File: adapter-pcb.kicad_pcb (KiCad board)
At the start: 2 copper layers, 90.2 x 95.9 mm, 27 parts, among them J1 SS5-80-3.50-L-D-K-TR, J2 DM3BT-DSF-PEJS, J3 Conn_02x05_Odd_Even, U1 TXS0102QDCURQ1, U2 LTC4300A-1IMS8_PBF

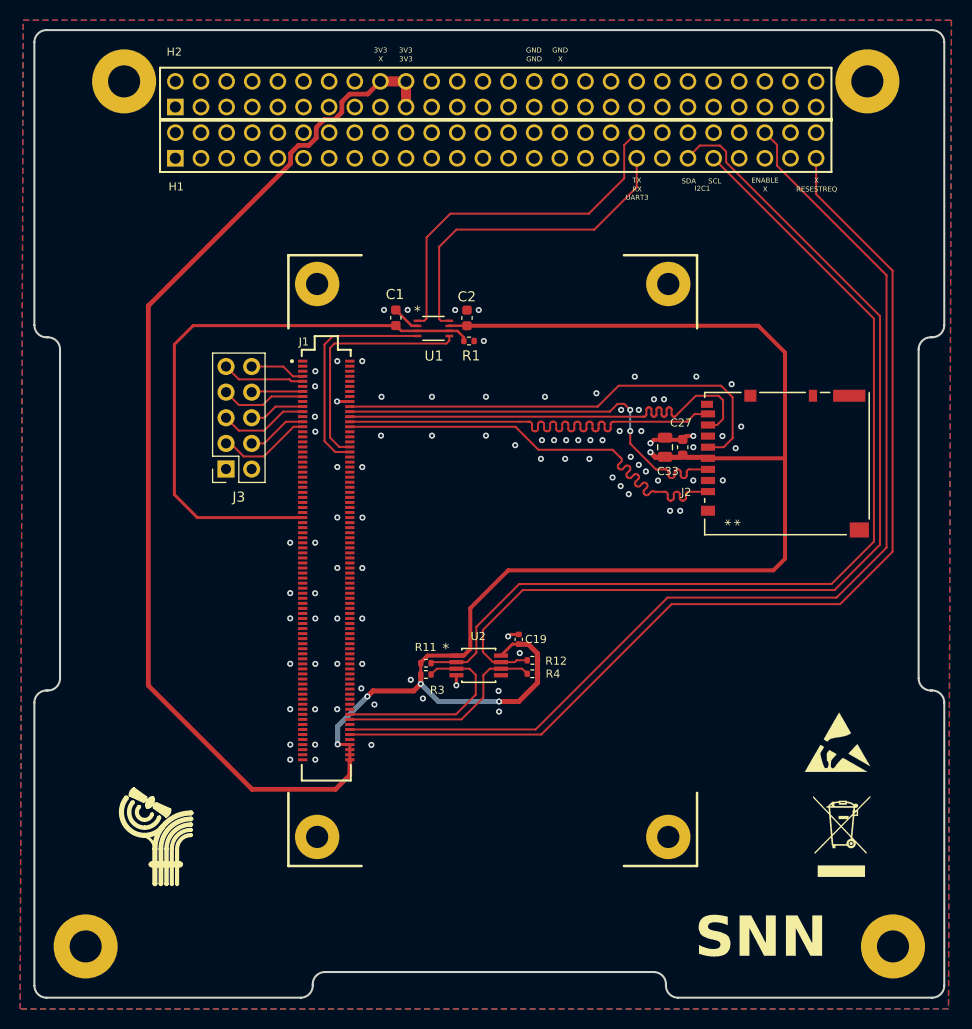
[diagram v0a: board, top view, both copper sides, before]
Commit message: Added some decoup caps and reviewed PCB layout
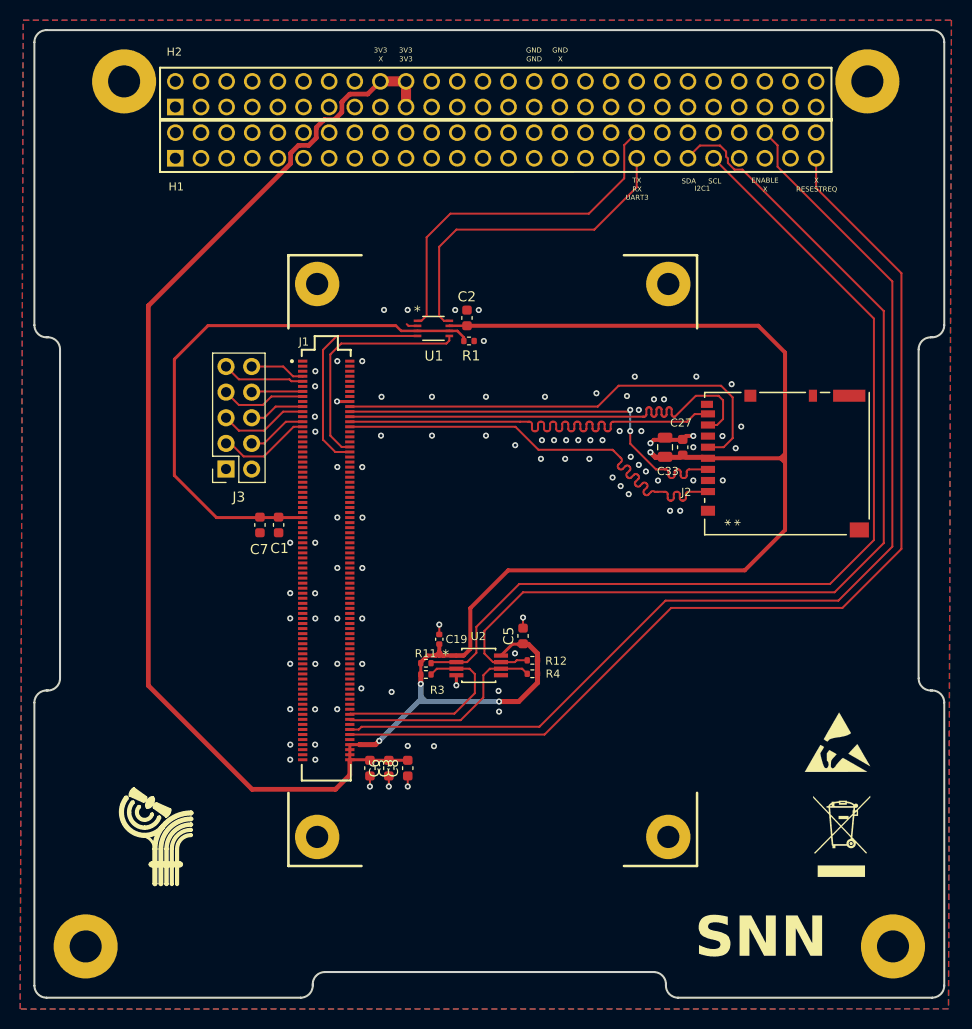
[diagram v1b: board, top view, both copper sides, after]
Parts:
- added C3: 100n, Capacitor_SMD:C_0603_1608Metric, F.Cu at (138.7, 119.6)
- added C5: 100n, Capacitor_SMD:C_0603_1608Metric, F.Cu at (153.8, 106.5)
- added C6: 100n, Capacitor_SMD:C_0603_1608Metric, F.Cu at (140.5, 119.6)
- added C7: 1uF, Capacitor_SMD:C_0603_1608Metric, F.Cu at (127.8, 95.5)
- added C8: 1uF, Capacitor_SMD:C_0603_1608Metric, F.Cu at (142.4, 119.6)
- moved C1 23.6 mm to (129.6, 95.5), turned to 90 degrees
- moved C19 7.88 mm to (145.5, 106.9)
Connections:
- MH5 pad 1: GND -> (no net)
- MH6 pad 1: GND -> (no net)
- MH7 pad 1: GND -> (no net)
- MH8 pad 1: GND -> (no net)
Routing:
- net +3V3: track 250.4 -> 258.0 mm
- net +1V8: track 58.8 -> 56.9 mm
- net GND: track 10.8 -> 12.2 mm, vias 91 -> 93
- net RESESTREQ: track 103.4 -> 104.5 mm
- net SNN Enable: track 106.8 -> 107.6 mm
- net I2C_SDA_CSKB: track 99.8 -> 100.5 mm
- net UART-RXD: track 23.8 -> 23.3 mm

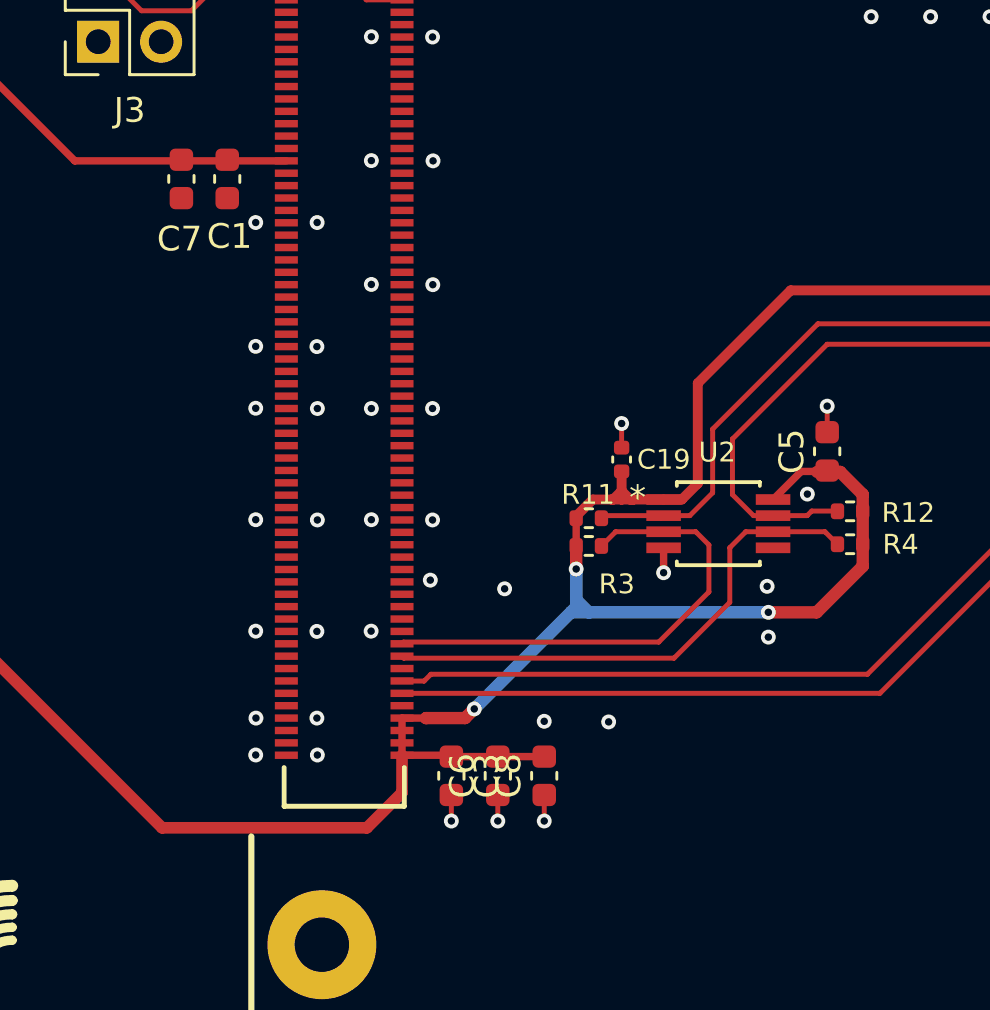
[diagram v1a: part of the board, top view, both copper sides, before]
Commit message: removed some decoup caps because I added to many haha
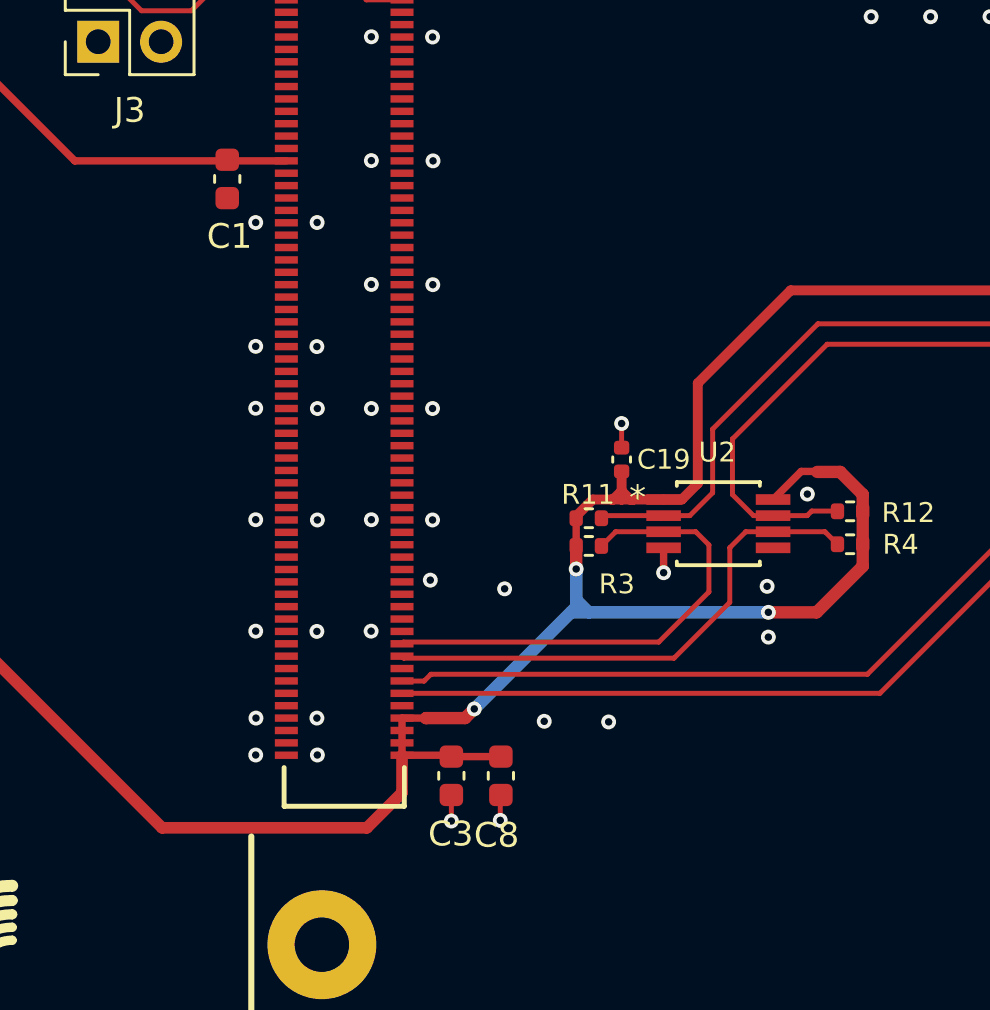
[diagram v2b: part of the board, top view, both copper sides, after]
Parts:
- removed C5, C6: 100n, Capacitor_SMD:C_0603_1608Metric
- removed C7: 1uF, Capacitor_SMD:C_0603_1608Metric
- moved C8 1.75 mm to (140.7, 119.6)
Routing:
- net +3V3: track 258.0 -> 255.2 mm, vias 5 -> 4
- net GND: track 12.2 -> 11.1 mm, vias 93 -> 92

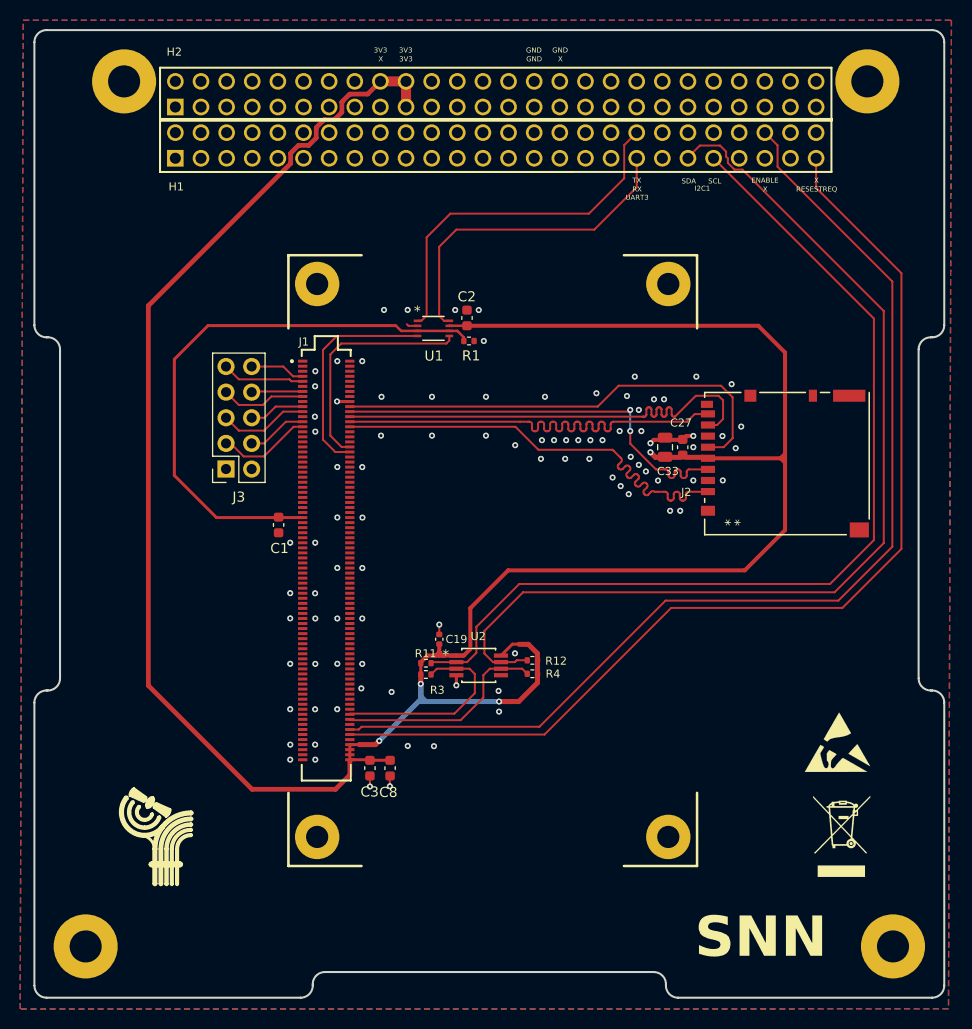
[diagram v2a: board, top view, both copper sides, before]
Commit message: Added Level Shifter for SD card
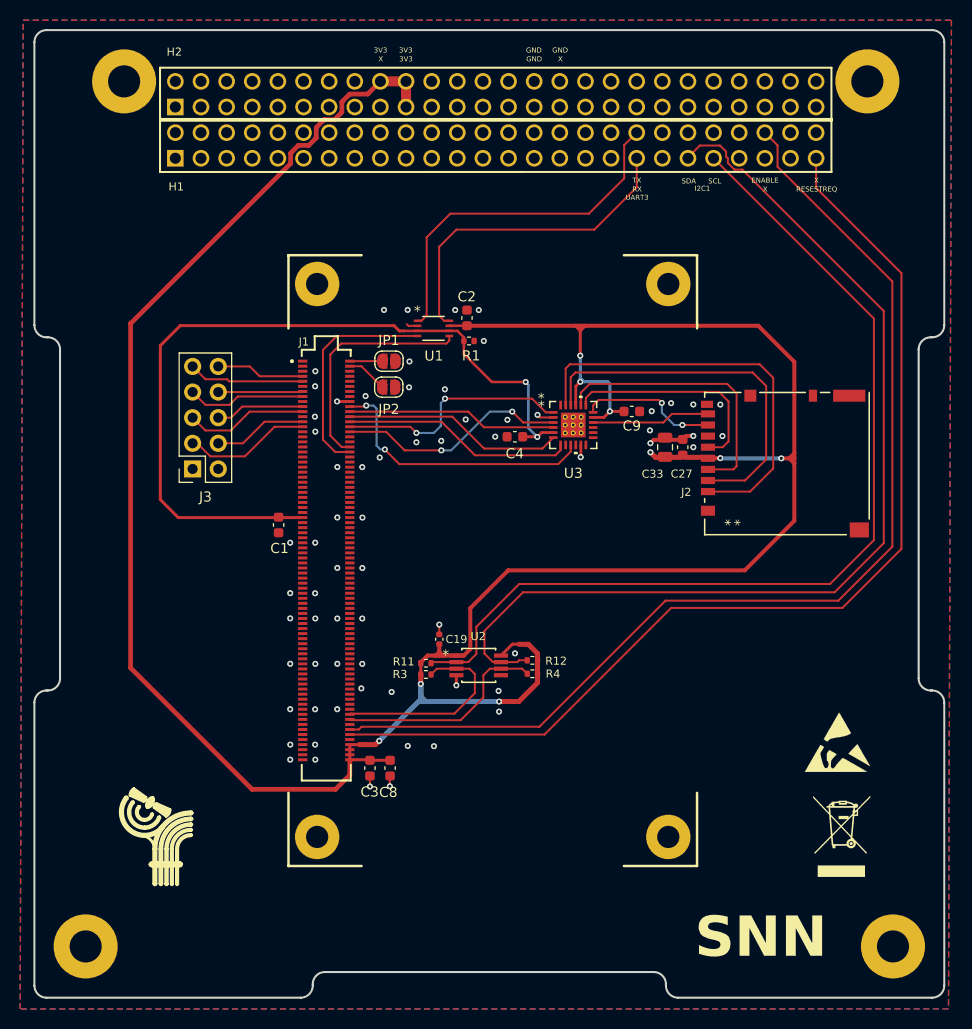
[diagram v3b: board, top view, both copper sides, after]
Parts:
- added C4: 100n, Capacitor_SMD:C_0603_1608Metric, F.Cu at (153.0, 86.8)
- added C9: 100n, Capacitor_SMD:C_0603_1608Metric, F.Cu at (164.6, 84.3)
- added JP1: SolderJumper_2_Open, Jumper:SolderJumper-2_P1.3mm_Open_RoundedPad1.0x1.5mm, F.Cu at (140.6, 79.3)
- added JP2: SolderJumper_2_Open, Jumper:SolderJumper-2_P1.3mm_Open_RoundedPad1.0x1.5mm, F.Cu at (140.5, 81.9)
- added U3: TXS02612RTWR, adapter:RTW24_2P45X2P45, F.Cu at (158.8, 85.6)
- MH1, MH2, MH3, MH4, MH5, MH6, MH7, MH8: value MountingHole_Pad_MP -> MountingHole_Pad
- moved J3 3.31 mm to (121.1, 90.0)
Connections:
- net I2C_SCL(2) renamed /I2C Buffer/I2C_SCL
- net I2C_SCL_CSKB renamed /CSKB/I2C_SCL_CSKB
- net I2C_SDA(2) renamed /I2C Buffer/I2C_SDA
- net I2C_SDA_CSKB renamed /CSKB/I2C_SDA_CSKB
- net RESESTREQ renamed /CSKB/RESETREQ
- net SNN Enable renamed /CSKB/ENABLE
- net UART-RXD renamed /TE0724 Connector/UART-RXD
- net UART-TXD renamed /TE0724 Connector/UART-TXD
- net UART_RX renamed /CSKB/UART-RXD LS
- net UART_TX renamed /CSKB/UART-TXD LS
- J1 pad 02: GND -> /TE0724 Connector/MODE1
- J1 pad 04: GND -> /TE0724 Connector/MODE0
- J1 pad 152: VBAT -> unconnected-(J1A-VBAT_OUT-Pad152)
- J1 pad 20: SD-CCLK -> /SD Level Shifter/SD-CCLK
- J1 pad 22: SD-CMD -> /SD Level Shifter/SD-CMD
- J1 pad 24: SD-D0 -> /SD Level Shifter/SD-D0
- J1 pad 26: SD-D1 -> /SD Level Shifter/SD-D1
- J1 pad 28: SD-D2 -> /SD Level Shifter/SD-D2
- J1 pad 30: SD-D3 -> /SD Level Shifter/SD-D3
- J1 pad 54: PWR_TEST -> unconnected-(J1A-VCCIO35-Pad54)
- J2 pad 1: SD-D2 -> /Micro SD/SD-D2 LS
- J2 pad 2: GND -> /Micro SD/SD-D3 LS
- J2 pad 3: SD-CMD -> /Micro SD/SD-CMD LS
- J2 pad 5: SD-CCLK -> /Micro SD/SD-CCLK LS
- J2 pad 7: SD-D0 -> /Micro SD/SD-D0 LS
- J2 pad 8: SD-D1 -> /Micro SD/SD-D1 LS
- MH1 pad 1: (no net) -> unconnected-(MH1-Pad1)
- MH2 pad 1: (no net) -> unconnected-(MH2-Pad1)
- MH3 pad 1: (no net) -> unconnected-(MH3-Pad1)
- MH4 pad 1: (no net) -> unconnected-(MH4-Pad1)
- MH5 pad 1: (no net) -> GND
- MH6 pad 1: (no net) -> GND
- MH7 pad 1: (no net) -> GND
- MH8 pad 1: (no net) -> GND
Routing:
- net SD-CCLK: track 46.1 -> 0.00 mm
- net SD-D0: track 46.0 -> 0.00 mm
- net SD-D2: track 45.9 -> 0.00 mm
- net SD-D1: track 45.9 -> 0.00 mm
- net SD-CMD: track 42.5 -> 0.00 mm, vias 2 -> 0
- net /Micro SD/SD-D2 LS: track 0.00 -> 41.3 mm
- net /Micro SD/SD-D3 LS: track 0.00 -> 36.8 mm
- net /SD Level Shifter/SD-CCLK: track 0.00 -> 27.7 mm, vias 0 -> 2
- net /Micro SD/SD-CMD LS: track 0.00 -> 27.6 mm
- net /SD Level Shifter/SD-D2: track 0.00 -> 23.7 mm, vias 0 -> 2
- net /SD Level Shifter/SD-D1: track 0.00 -> 23.0 mm
- net /SD Level Shifter/SD-D3: track 0.00 -> 23.0 mm, vias 0 -> 2
- net +1V8: track 56.9 -> 79.6 mm, vias 0 -> 2
- net +3V3: track 255.2 -> 277.6 mm, vias 4 -> 9
- net /SD Level Shifter/SD-D0: track 0.00 -> 21.9 mm
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
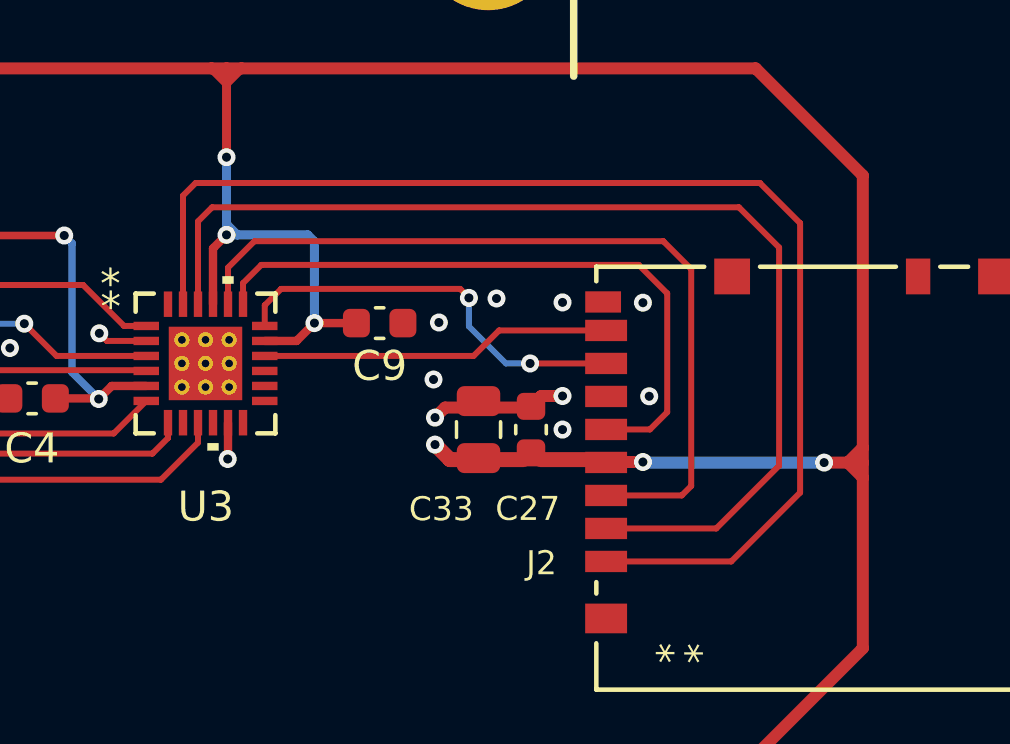
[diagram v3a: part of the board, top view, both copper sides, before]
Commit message: Rerouted SD a little bit
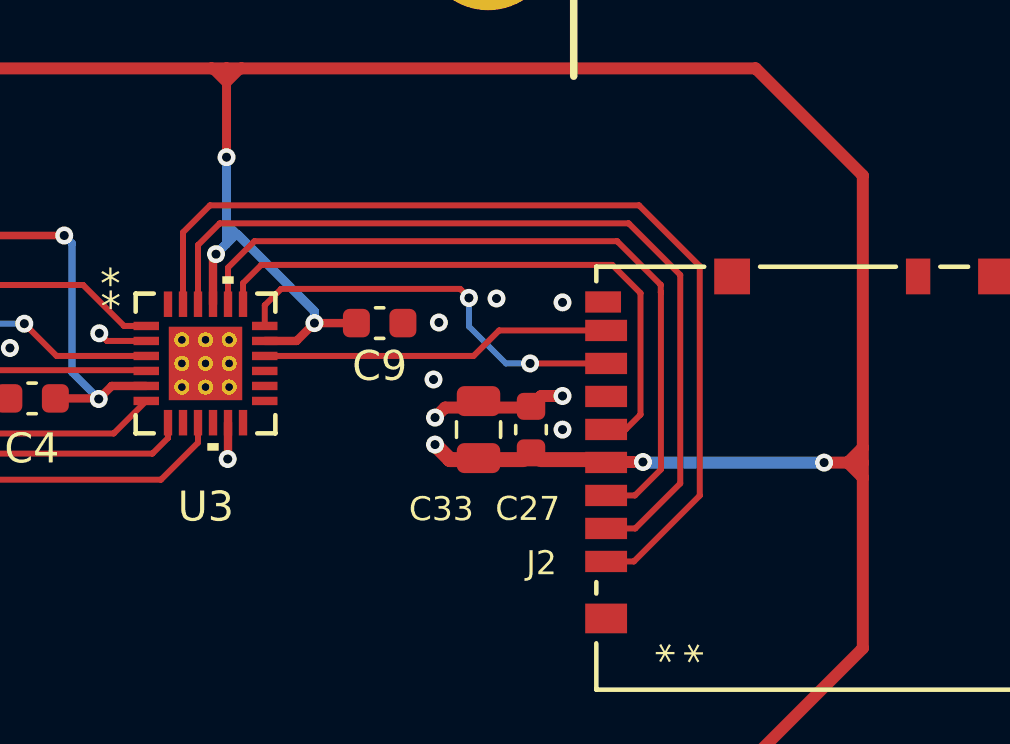
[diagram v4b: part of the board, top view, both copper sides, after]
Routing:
- net /Micro SD/SD-D2 LS: track 41.3 -> 32.5 mm
- net /Micro SD/SD-D3 LS: track 36.8 -> 29.1 mm
- net /Micro SD/SD-CMD LS: track 27.6 -> 25.0 mm
- net /Micro SD/SD-CCLK LS: track 21.7 -> 20.0 mm
- net +3V3: track 277.6 -> 276.9 mm
- net GND: vias 67 -> 65
